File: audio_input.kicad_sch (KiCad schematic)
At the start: 64 parts, among them J12 NCJ6FA-H-0, J13 NCJ6FA-H-0, Q1 2N3904, Q2 2N3904, Q3 2N3906, Q4 2N3906, U10 THAT1246, U11 THAT1246, U8 OPA1656ID, U9 LM2903

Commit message: fix seed schematic
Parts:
- renumbered J12 to J11, J13 to J12, RV7 to RV3, RV8 to RV4

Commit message: footprints fixed
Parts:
- TP1, TP10, TP2, TP3, TP4, TP5, TP6, TP7, TP8, TP9: footprint (none) -> TestPoint:TestPoint_Pad_1.5x1.5mm
- U9: footprint (none) -> Package_SO:SOIC-8_3.9x4.9mm_P1.27mm
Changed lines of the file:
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@@
 			)
 		)
-		(property "Footprint" ""
+		(property "Footprint" "TestPoint:TestPoint_Pad_1.5x1.5mm"
 			(at 73.66 106.68 0)
 			(effects
@@
 			)
 		)
-		(property "Footprint" ""
+		(property "Footprint" "TestPoint:TestPoint_Pad_1.5x1.5mm"
 			(at 53.34 45.72 0)
 			(effects
@@
 			)
 		)
-		(property "Footprint" ""
+		(property "Footprint" "TestPoint:TestPoint_Pad_1.5x1.5mm"
 			(at 53.34 107.95 0)
 			(effects
@@
 			)
 		)
-		(property "Footprint" ""
+		(property "Footprint" "Package_SO:SOIC-8_3.9x4.9mm_P1.27mm"
 			(at 40.64 176.53 0)
 			(effects
@@
 			)
 		)
-		(property "Footprint" ""
+		(property "Footprint" "TestPoint:TestPoint_Pad_1.5x1.5mm"
 			(at 109.22 46.99 0)
 			(effects
@@
 			)
 		)
-		(property "Footprint" ""
+		(property "Footprint" "TestPoint:TestPoint_Pad_1.5x1.5mm"
 			(at 53.34 43.18 0)
 			(effects
@@
 			)
 		)
-		(property "Footprint" ""
+		(property "Footprint" "TestPoint:TestPoint_Pad_1.5x1.5mm"
 			(at 109.22 109.22 0)
 			(effects
@@
 			)
 		)
-		(property "Footprint" ""
+		(property "Footprint" "TestPoint:TestPoint_Pad_1.5x1.5mm"
 			(at 142.24 109.22 0)
 			(effects
@@
 			)
 		)
-		(property "Footprint" ""
+		(property "Footprint" "Package_SO:SOIC-8_3.9x4.9mm_P1.27mm"
 			(at 189.23 118.11 0)
 			(effects
@@
 			)
 		)
-		(property "Footprint" ""
+		(property "Footprint" "Package_SO:SOIC-8_3.9x4.9mm_P1.27mm"
 			(at 189.23 55.88 0)
 			(effects
@@
 			)
 		)
-		(property "Footprint" ""
+		(property "Footprint" "TestPoint:TestPoint_Pad_1.5x1.5mm"
 			(at 142.24 46.99 0)
 			(effects
@@
 			)
 		)
-		(property "Footprint" ""
+		(property "Footprint" "TestPoint:TestPoint_Pad_1.5x1.5mm"
 			(at 74.93 44.45 0)
 			(effects
@@
 			)
 		)
-		(property "Footprint" ""
+		(property "Footprint" "TestPoint:TestPoint_Pad_1.5x1.5mm"
 			(at 53.34 105.41 0)
 			(effects

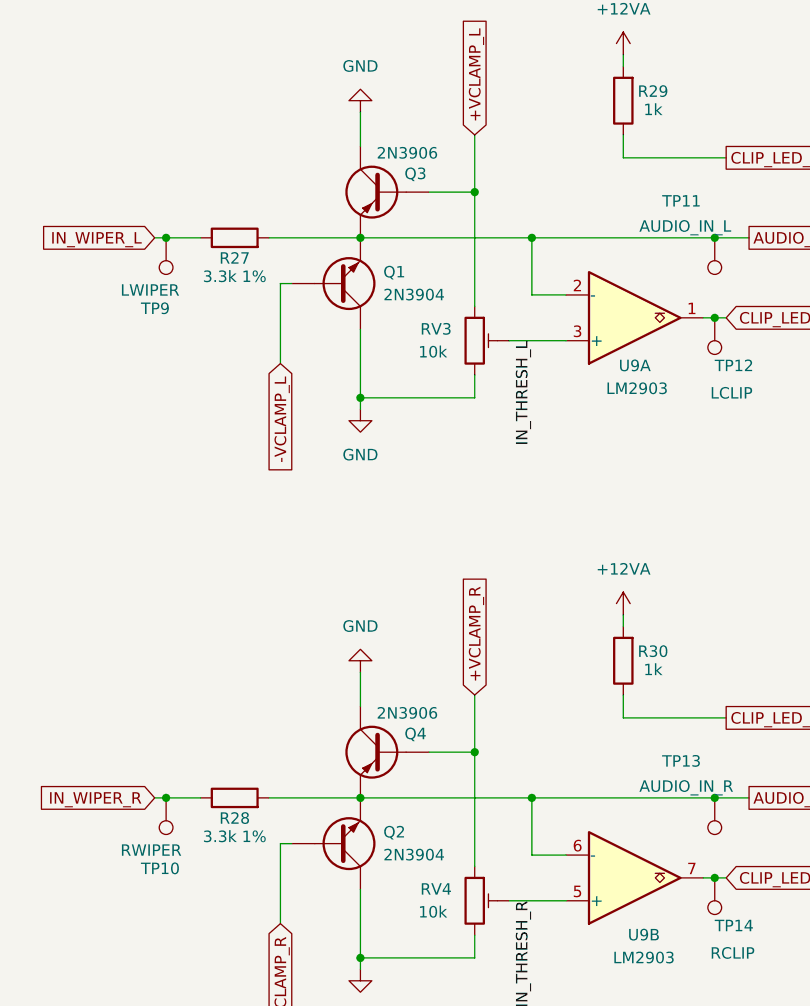
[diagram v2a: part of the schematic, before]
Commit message: reannotate, fix cap footprints
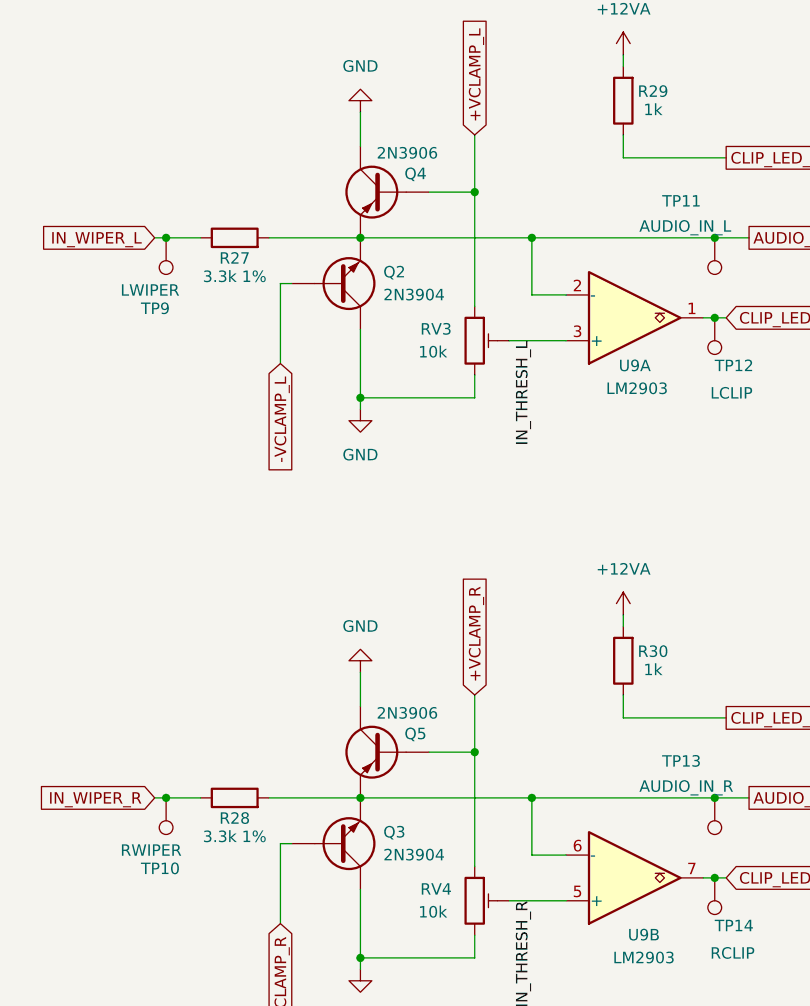
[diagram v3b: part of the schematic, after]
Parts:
- renumbered Q1 to Q2, Q2 to Q3, Q3 to Q4, Q4 to Q5
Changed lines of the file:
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@@
 		(on_board yes)
 		(dnp no)
-		(property "Reference" "Q4"
+		(property "Reference" "Q5"
 			(at 166.116 102.108 0)
 			(effects
@@
 			(project "daisy-studio"
 				(path "/55cca6a8-30da-4c13-b2f2-a01401e2b54c/a1b2c3d4-7777-4000-8000-000000000007"
-					(reference "Q4")
+					(reference "Q5")
 					(unit 1)
 				)
@@
 		(on_board yes)
 		(dnp no)
-		(property "Reference" "Q1"
+		(property "Reference" "Q2"
 			(at 161.29 50.7999 0)
 			(effects
@@
 			(project "daisy-studio"
 				(path "/55cca6a8-30da-4c13-b2f2-a01401e2b54c/a1b2c3d4-7777-4000-8000-000000000007"
-					(reference "Q1")
+					(reference "Q2")
 					(unit 1)
 				)
@@
 		(on_board yes)
 		(dnp no)
-		(property "Reference" "Q3"
+		(property "Reference" "Q4"
 			(at 166.116 39.878 0)
 			(effects
@@
 			(project "daisy-studio"
 				(path "/55cca6a8-30da-4c13-b2f2-a01401e2b54c/a1b2c3d4-7777-4000-8000-000000000007"
-					(reference "Q3")
+					(reference "Q4")
 					(unit 1)
 				)
@@
 		(on_board yes)
 		(dnp no)
-		(property "Reference" "Q2"
+		(property "Reference" "Q3"
 			(at 161.29 113.0299 0)
 			(effects
@@
 			(project "daisy-studio"
 				(path "/55cca6a8-30da-4c13-b2f2-a01401e2b54c/a1b2c3d4-7777-4000-8000-000000000007"
-					(reference "Q2")
+					(reference "Q3")
 					(unit 1)
 				)

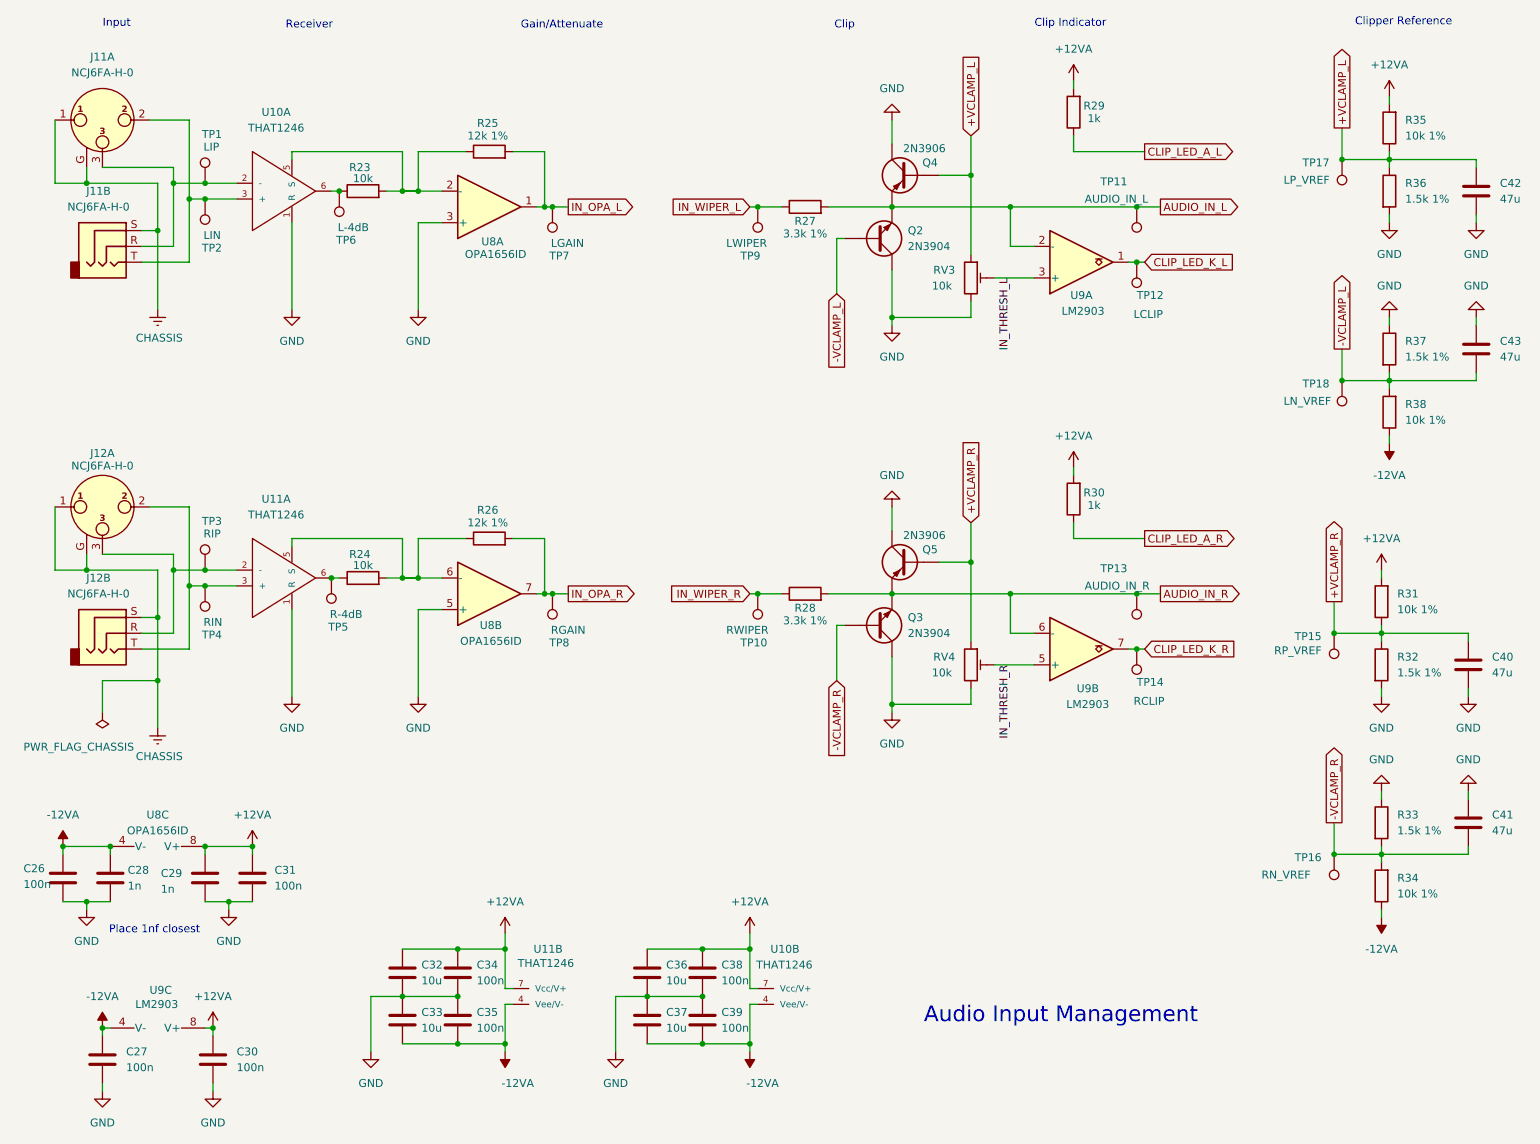
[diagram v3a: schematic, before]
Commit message: change docs to use RS3-1212D
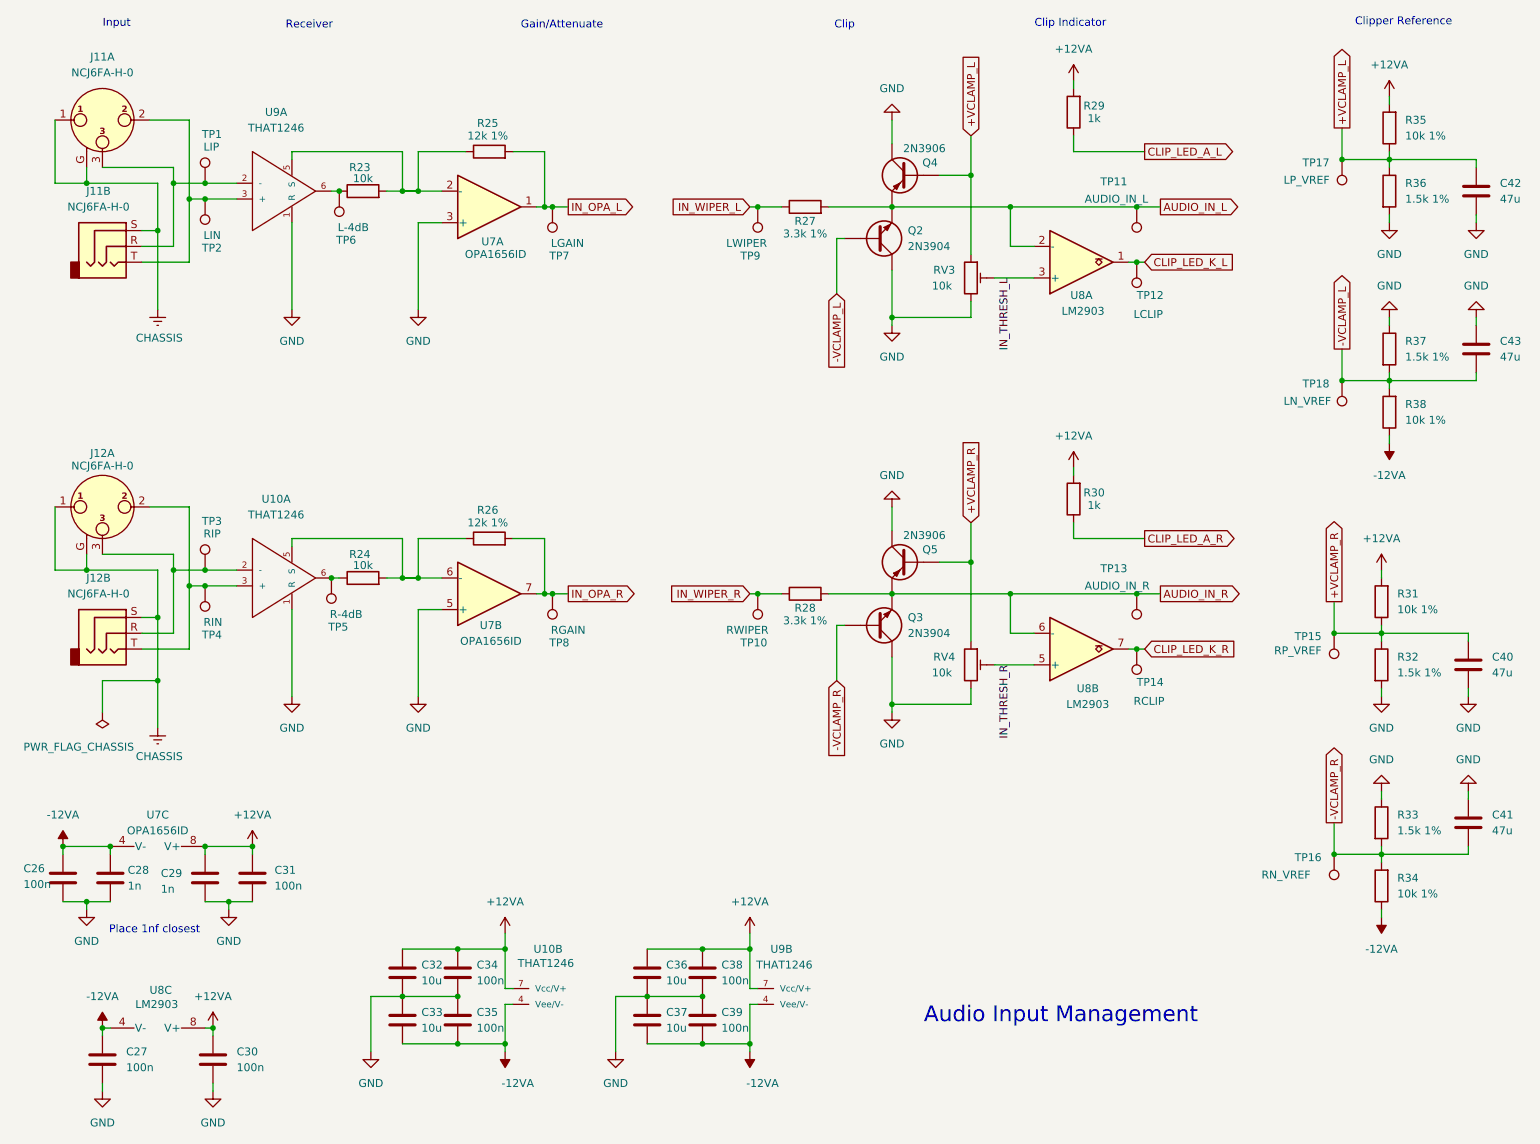
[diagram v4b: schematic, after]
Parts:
- renumbered U11 to U10, U8 to U7, U9 to U8, U10 to U9

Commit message: lots of pcb work
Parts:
- removed TP1: LIP, TestPoint:TestPoint_Pad_1.5x1.5mm, symbol Connector:TestPoint
- removed TP10: RWIPER, TestPoint:TestPoint_Pad_1.5x1.5mm, symbol Connector:TestPoint
- removed TP11: AUDIO_IN_L, TestPoint:TestPoint_Pad_1.5x1.5mm, symbol Connector:TestPoint
- removed TP12: LCLIP, TestPoint:TestPoint_Pad_1.5x1.5mm, symbol Connector:TestPoint
- removed TP13: AUDIO_IN_R, TestPoint:TestPoint_Pad_1.5x1.5mm, symbol Connector:TestPoint
- removed TP14: RCLIP, TestPoint:TestPoint_Pad_1.5x1.5mm, symbol Connector:TestPoint
- removed TP15: RP_VREF, TestPoint:TestPoint_Pad_1.5x1.5mm, symbol Connector:TestPoint
- removed TP16: RN_VREF, TestPoint:TestPoint_Pad_1.5x1.5mm, symbol Connector:TestPoint
- removed TP17: LP_VREF, TestPoint:TestPoint_Pad_1.5x1.5mm, symbol Connector:TestPoint
- removed TP18: LN_VREF, TestPoint:TestPoint_Pad_1.5x1.5mm, symbol Connector:TestPoint
- removed TP2: LIN, TestPoint:TestPoint_Pad_1.5x1.5mm, symbol Connector:TestPoint
- removed TP3: RIP, TestPoint:TestPoint_Pad_1.5x1.5mm, symbol Connector:TestPoint
- removed TP4: RIN, TestPoint:TestPoint_Pad_1.5x1.5mm, symbol Connector:TestPoint
- removed TP5: R-4dB, TestPoint:TestPoint_Pad_1.5x1.5mm, symbol Connector:TestPoint
- removed TP6: L-4dB, TestPoint:TestPoint_Pad_1.5x1.5mm, symbol Connector:TestPoint
- removed TP7: LGAIN, TestPoint:TestPoint_Pad_1.5x1.5mm, symbol Connector:TestPoint
- removed TP8: RGAIN, TestPoint:TestPoint_Pad_1.5x1.5mm, symbol Connector:TestPoint
- removed TP9: LWIPER, TestPoint:TestPoint_Pad_1.5x1.5mm, symbol Connector:TestPoint
- Q2, Q3: value 2N3904 -> MMBT3904; footprint Package_TO_SOT_THT:TO-92_Inline -> Package_TO_SOT_SMD:SOT-23
- Q4, Q5: value 2N3906 -> MMBT3906; footprint Package_TO_SOT_THT:TO-92_Inline -> Package_TO_SOT_SMD:SOT-23

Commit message: lots of pcb work
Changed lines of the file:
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@@
 		(color 0 0 0 0)
+	)
+	(bus_entry
+		(at 60.96 17.78)
+		(size 2.54 2.54)
+		(stroke
+			(width 0)
+			(type default)
+		)
 	)
 	(wire

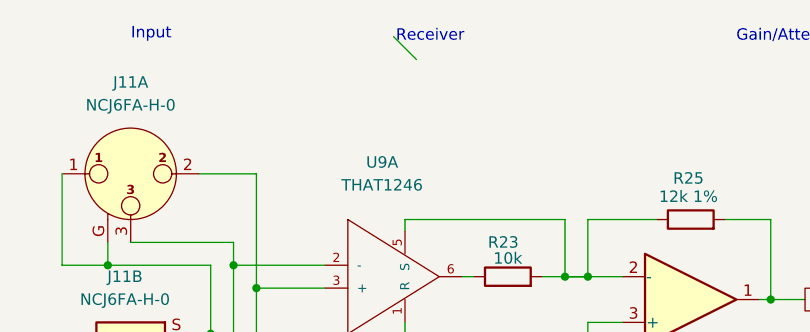
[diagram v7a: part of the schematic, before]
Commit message: clean up some power cap issues
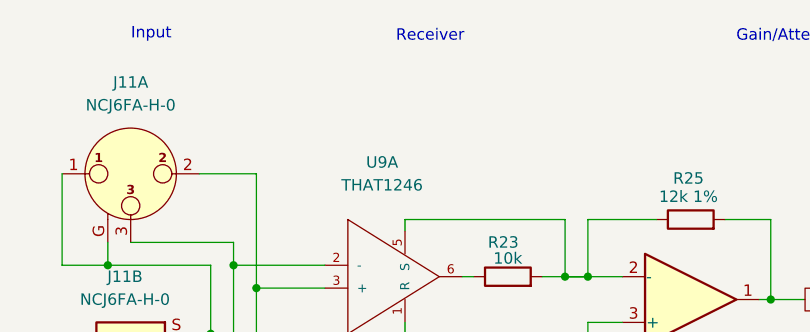
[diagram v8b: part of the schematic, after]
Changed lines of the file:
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@@
 		(color 0 0 0 0)
-	)
-	(bus_entry
-		(at 60.96 17.78)
-		(size 2.54 2.54)
-		(stroke
-			(width 0)
-			(type default)
-		)
 	)
 	(wire
